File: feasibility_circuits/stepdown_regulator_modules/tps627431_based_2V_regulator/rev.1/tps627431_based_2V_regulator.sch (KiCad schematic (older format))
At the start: 32 parts, among them J1 TEST, J2 VSEL1_HIGH, J3 VSEL1_LOW, J4 VSEL2_LOW, J5 VSEL2_HIGH, J6 VSEL3_HIGH, J7 VSEL3_LOW, J8 TEST, J9 TEST, P1 VIN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

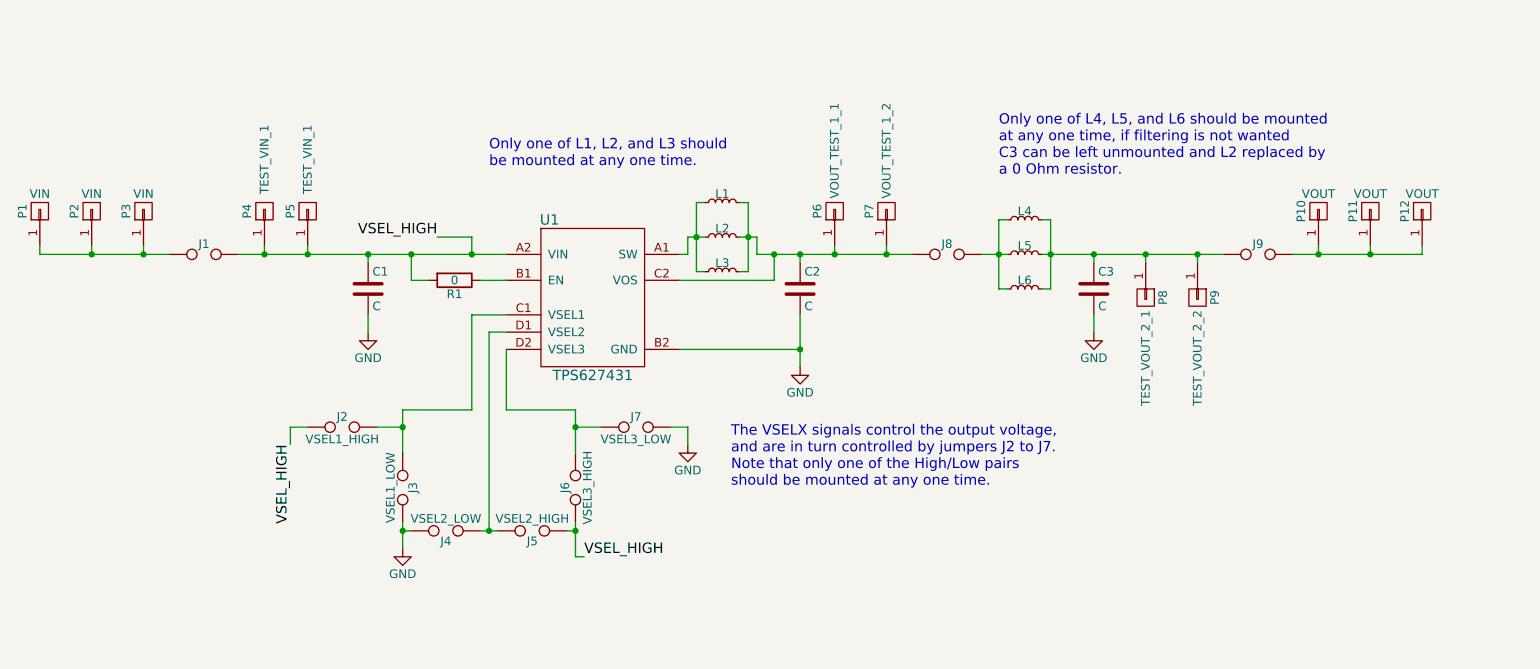
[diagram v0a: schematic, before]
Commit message: Completed intial draft of TPS627431 2V regulator prototype board
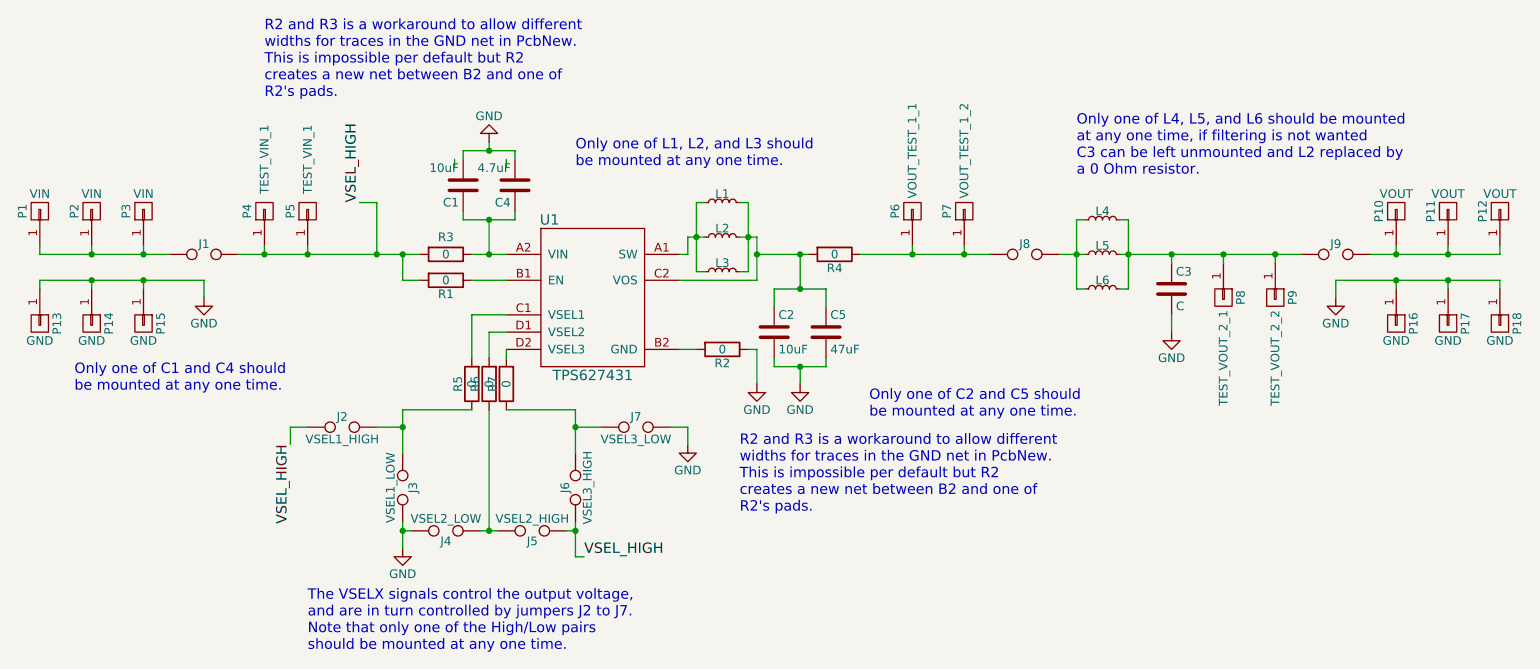
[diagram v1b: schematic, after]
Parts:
- added C4: 4.7uF, Capacitors_SMD:C_0402, symbol C
- added C5: 47uF, Capacitors_SMD:C_0805_HandSoldering, symbol C
- added P13, P14, P15, P16, P17, P18: GND, custom_connectors:proto_pad-square-3mm, symbol CONN_01X01
- added R2, R3, R4, R5, R6, R7: 0, Resistors_SMD:R_0805_HandSoldering, symbol R
- C1, C2: value C -> 10uF; footprint (none) -> Capacitors_SMD:C_0805_HandSoldering
- C3: footprint (none) -> Capacitors_SMD:C_0805_HandSoldering
- J1, J2, J3, J4, J5, J6, J7, J8, J9: footprint (none) -> custom_connectors:proto_header-vt-1x2-2.54mm-G_C__SABN_M30
- L1: footprint (none) -> custom_inductors:proto_inductor-WE_74404043100A_455x360
- L2, L6: footprint (none) -> custom_inductors:proto_inductor-smd_1210
- L3: footprint (none) -> custom_inductors:proto_inductor-WE_74404064220_640x570
- L4: footprint (none) -> custom_inductors:proto_inductor-smd_1008
- L5: footprint (none) -> custom_inductors:proto_inductor-smd_0805
- P1, P10, P11, P12, P2, P3, P4, P5, P6, P7, P8, P9: footprint (none) -> custom_connectors:proto_pad-square-3mm
- R1: footprint (none) -> Resistors_SMD:R_0805_HandSoldering
- U1: footprint (none) -> custom_amplifiers:proto_amp-ti_tps624731
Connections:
- wire segments 70 -> 98
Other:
- note added: "Only one of C1 and C4 should \nbe mounted at any one time."
- note added: "Only one of C2 and C5 should \nbe mounted at any one time."
- note added: "R2 and R3 is a workaround to allow different \nwidths for traces in the GND net in PcbNew. \nThis is impossible per default but R2 \ncreates a new net between B2 and one of \nR2's pads."
- moved on the sheet: C1, C2, C3, J8, J9, L4, L5, L6, P10, P11, P12, P6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
